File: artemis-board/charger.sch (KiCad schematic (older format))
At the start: 24 parts, among them J10 External NTC, J2 Thermistor, Q2 2N7002, SW2 SKRKAEE020, U3 LC709203FQH-01TWG, U4 TP4056, U8 XC6206P332MR

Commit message: connected VccP of io expander back to 3v3, changed some footprint
also added NMos so voltage divider can be used
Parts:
- R7: footprint Resistor_SMD:R_0603_1608Metric_Pad1.05x0.95mm_HandSolder -> Resistor_SMD:R_0603_1608Metric_Pad0.98x0.95mm_HandSolder
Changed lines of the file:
@@
 F 0 "R7" H 7100 3150 50  0000 L CNN
 F 1 "1M" H 7100 3250 50  0000 L CNN
-F 2 "Resistor_SMD:R_0603_1608Metric_Pad1.05x0.95mm_HandSolder" V 7180 3200 50  0001 C CNN
+F 2 "Resistor_SMD:R_0603_1608Metric_Pad0.98x0.95mm_HandSolder" V 7180 3200 50  0001 C CNN
 F 3 "~" H 7250 3200 50  0001 C CNN
 F 4 "C22935" H 7250 3200 50  0001 C CNN "LCSC"

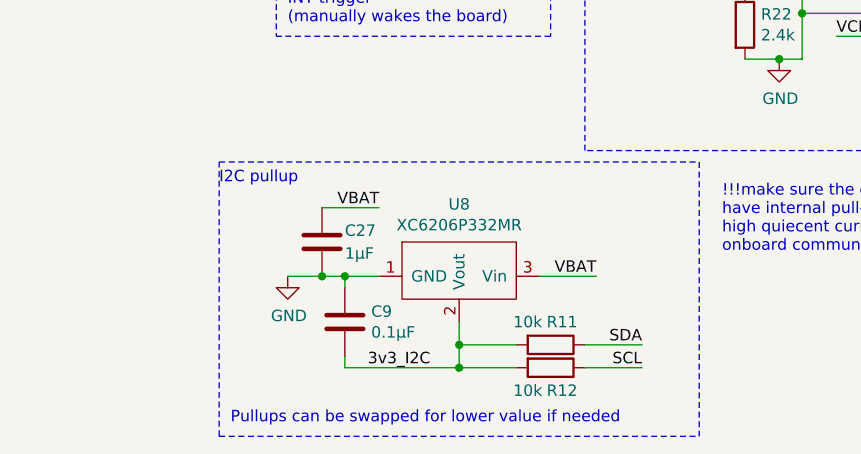
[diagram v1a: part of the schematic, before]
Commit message: added cap to 3v3 I2c, swapped some footprints to normal...
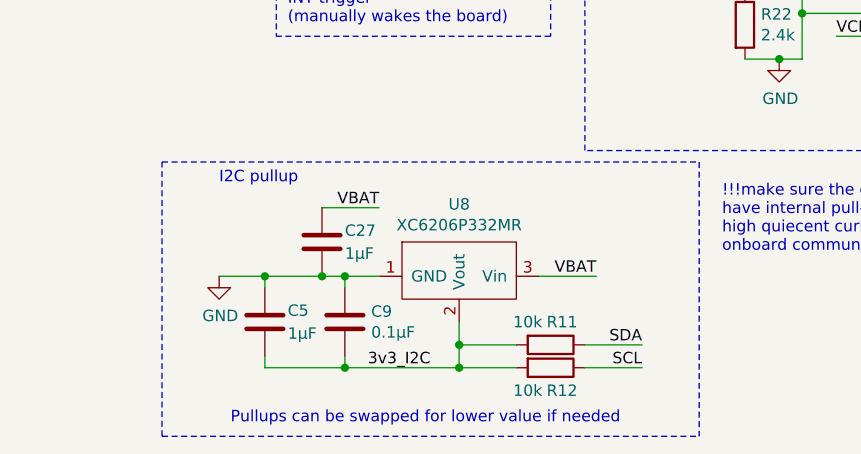
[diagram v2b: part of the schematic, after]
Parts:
- added C5: 1µF, Capacitor_SMD:C_0603_1608Metric_Pad1.08x0.95mm_HandSolder, symbol Device:C
- TP4: DNP (none) -> DNP
- U8: footprint Package_TO_SOT_SMD:SOT-23_Handsoldering -> Package_TO_SOT_SMD:SOT-23
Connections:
- net 3v3_I2C: now also C5.2
- net GND: now also C5.1
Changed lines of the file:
@@
 F 2 "TestPoint:TestPoint_Pad_1.5x1.5mm" H 6550 5050 50  0001 C CNN
 F 3 "~" H 6550 5050 50  0001 C CNN
+F 4 "DNP" H 6350 5050 50  0001 C CNN "DNP"
 	1    6350 5050
 	1    0    0    -1
@@
 I2C pullup\n
 Wire Notes Line
-	2250 7250 4350 7250
-Wire Notes Line
-	2250 7250 2250 6050
+	2000 7250 2000 6050
 Wire Notes Line
 	4350 6050 4350 7250
-Wire Notes Line
-	2250 6050 4350 6050
 Wire Wire Line
 	3650 6550 3900 6550
@@
 L power:GND #PWR?
 U 1 1 6026DD90
-P 2550 6550
+P 2250 6550
 AR Path="/5F63A00B/6026DD90" Ref="#PWR?"  Part="1"
 AR Path="/5F63A0E9/6026DD90" Ref="#PWR?"  Part="1"
 AR Path="/5F639F48/6026DD90" Ref="#PWR0108"  Part="1"
-F 0 "#PWR0108" H 2550 6300 50  0001 C CNN
-F 1 "GND" H 2555 6377 50  0000 C CNN
-F 2 "" H 2550 6550 50  0001 C CNN
-F 3 "" H 2550 6550 50  0001 C CNN
-	1    2550 6550
+F 0 "#PWR0108" H 2250 6300 50  0001 C CNN
+F 1 "GND" H 2255 6377 50  0000 C CNN
+F 2 "" H 2250 6550 50  0001 C CNN
+F 3 "" H 2250 6550 50  0001 C CNN
+	1    2250 6550
 	1    0    0    -1
 $EndComp
@@
 F 0 "U8" H 3300 6665 50  0000 C CNN
 F 1 "XC6206P332MR" H 3300 6574 50  0000 C CNN
-F 2 "Package_TO_SOT_SMD:SOT-23_Handsoldering" H 3350 6100 50  0001 C CNN
+F 2 "Package_TO_SOT_SMD:SOT-23" H 3350 6100 50  0001 C CNN
 F 3 "https://www.torexsemi.com/file/xc6206/XC6206.pdf" H 3500 6450 50  0001 C CNN
 F 4 "C5446" H 3300 6450 50  0001 C CNN "LCSC"
@@
 Connection ~ 2700 6550
 Wire Wire Line
-	2700 6550 2550 6550
+	2700 6550 2450 6550
 Wire Wire Line
 	2700 6250 2950 6250
 Text Label 2950 6250 2    50   ~ 0
 VBAT
+$Comp
+L Device:C C5
+U 1 1 60EBFB71
+P 2450 6750
+F 0 "C5" H 2550 6800 50  0000 L CNN
+F 1 "1µF" H 2550 6700 50  0000 L CNN
+F 2 "Capacitor_SMD:C_0603_1608Metric_Pad1.08x0.95mm_HandSolder" H 2488 6600 50  0001 C CNN
+F 3 "~" H 2450 6750 50  0001 C CNN
+F 4 "C15849" H 2450 6750 50  0001 C CNN "LCSC"
+	1    2450 6750
+	1    0    0    -1
+$EndComp
+Wire Wire Line
+	2450 6600 2450 6550
+Connection ~ 2450 6550
+Wire Wire Line
+	2450 6550 2250 6550
+Wire Wire Line
+	2450 6900 2450 6950
+Wire Wire Line
+	2450 6950 2800 6950
+Connection ~ 2800 6950
+Wire Notes Line
+	2000 7250 4350 7250
+Wire Notes Line
+	2000 6050 4350 6050
 $EndSCHEMATC

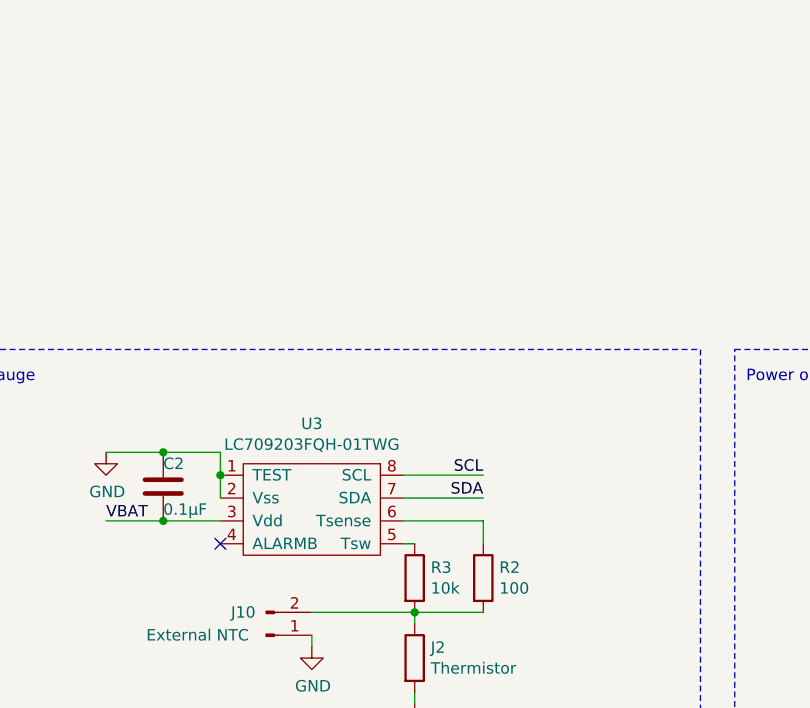
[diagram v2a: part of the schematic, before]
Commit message: added WLCSP9 footprint for LC709203
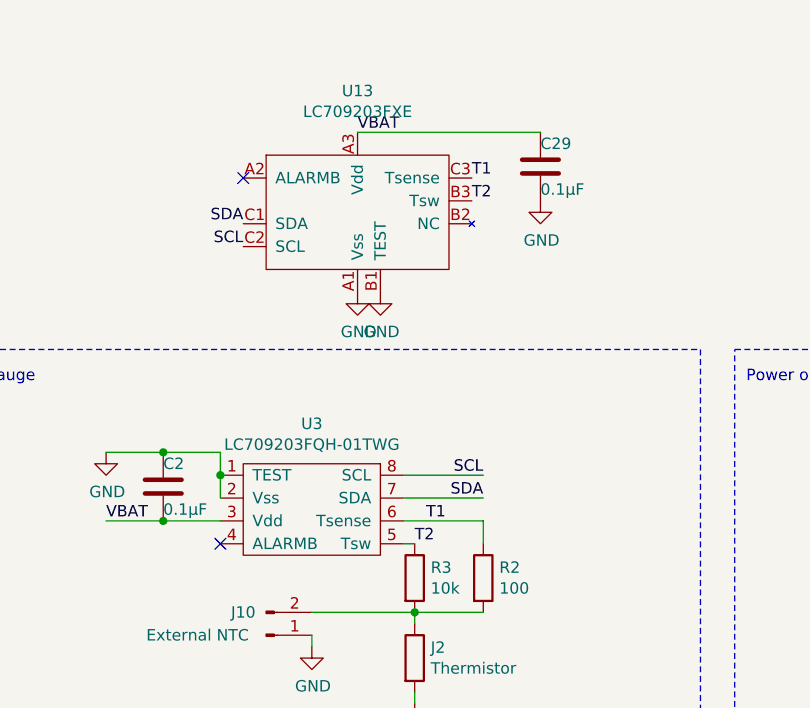
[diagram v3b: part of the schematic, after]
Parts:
- added C29: 0.1µF, Capacitor_SMD:C_0603_1608Metric_Pad1.05x0.95mm_HandSolder, symbol Device:C
- added U13: LC709203FXE, Package_CSP:WLCSP-9_3x3_1.76x1.6mm, symbol LC709203FQH:LC709203FXE
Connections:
- net GND: now also C29.2, U13.A1 (Vss), U13.B1 (TEST)
- net SCL: now also U13.C2 (SCL)
- net SDA: now also U13.C1 (SDA)
- net VBAT: now also C29.1, U13.A3 (Vdd)
- net T2: now reaches R3.1, U3.5 (Tsw)
- net T2: now also U13.B3 (Tsw)
- net T1: now reaches R2.1, U3.6 (Tsense)
- net T1: now also U13.C3 (Tsense)
- no-connect marks 1 -> 2
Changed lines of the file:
@@
 Wire Notes Line
 	2000 6050 4350 6050
+$Comp
+L LC709203FQH:LC709203FXE U13
+U 1 1 61073159
+P 4400 1550
+F 0 "U13" H 4400 2181 50  0000 C CNN
+F 1 "LC709203FXE" H 4400 2090 50  0000 C CNN
+F 2 "Package_CSP:WLCSP-9_3x3_1.76x1.6mm" H 4400 2150 50  0001 C CNN
+F 3 "https://www.onsemi.com/pub/Collateral/LC709203F-D.PDF" H 4400 2150 50  0001 C CNN
+F 4 "DNP" H 4400 1550 50  0001 C CNN "DNP"
+F 5 "C184366" H 4400 1550 50  0001 C CNN "LCSC"
+	1    4400 1550
+	1    0    0    -1
+$EndComp
+$Comp
+L power:GND #PWR0120
+U 1 1 6107483E
+P 4400 1800
+F 0 "#PWR0120" H 4400 1550 50  0001 C CNN
+F 1 "GND" H 4405 1627 50  0000 C CNN
+F 2 "" H 4400 1800 50  0001 C CNN
+F 3 "" H 4400 1800 50  0001 C CNN
+	1    4400 1800
+	1    0    0    -1
+$EndComp
+Text Label 4400 1100 0    50   ~ 0
+VBAT
+Text Label 3900 1600 2    50   ~ 0
+SCL
+Text Label 3900 1500 2    50   ~ 0
+SDA
+$Comp
+L power:GND #PWR0121
+U 1 1 610782C0
+P 4500 1800
+F 0 "#PWR0121" H 4500 1550 50  0001 C CNN
+F 1 "GND" H 4505 1627 50  0000 C CNN
+F 2 "" H 4500 1800 50  0001 C CNN
+F 3 "" H 4500 1800 50  0001 C CNN
+	1    4500 1800
+	1    0    0    -1
+$EndComp
+NoConn ~ 3900 1300
+Text Label 4700 2800 0    50   ~ 0
+T1
+Text Label 4650 2900 0    50   ~ 0
+T2
+Text Label 4900 1400 0    50   ~ 0
+T2
+Text Label 4900 1300 0    50   ~ 0
+T1
+$Comp
+L Device:C C29
+U 1 1 6108341B
+P 5200 1250
+F 0 "C29" H 5200 1350 50  0000 L CNN
+F 1 "0.1µF" H 5200 1150 50  0000 L CNN
+F 2 "Capacitor_SMD:C_0603_1608Metric_Pad1.05x0.95mm_HandSolder" H 5238 1100 50  0001 C CNN
+F 3 "~" H 5200 1250 50  0001 C CNN
+F 4 "C14858" H 5200 1250 50  0001 C CNN "LCSC"
+	1    5200 1250
+	1    0    0    -1
+$EndComp
+Wire Wire Line
+	5200 1100 4400 1100
+$Comp
+L power:GND #PWR?
+U 1 1 6108AFC4
+P 5200 1400
+F 0 "#PWR?" H 5200 1150 50  0001 C CNN
+F 1 "GND" H 5205 1227 50  0000 C CNN
+F 2 "" H 5200 1400 50  0001 C CNN
+F 3 "" H 5200 1400 50  0001 C CNN
+	1    5200 1400
+	1    0    0    -1
+$EndComp
 $EndSCHEMATC
